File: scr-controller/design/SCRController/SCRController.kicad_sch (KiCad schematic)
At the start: 43 parts, among them J1 VALT, J2 SAL_TRIAC, Q1 2N2907A, Q2 2N2222A, Q3 2N2222A, Q4 2N2907A, U1 TL084, U2 TL084, U3 LM7815_TO220, U4 LM7915_TO220, U5 MOC3011M

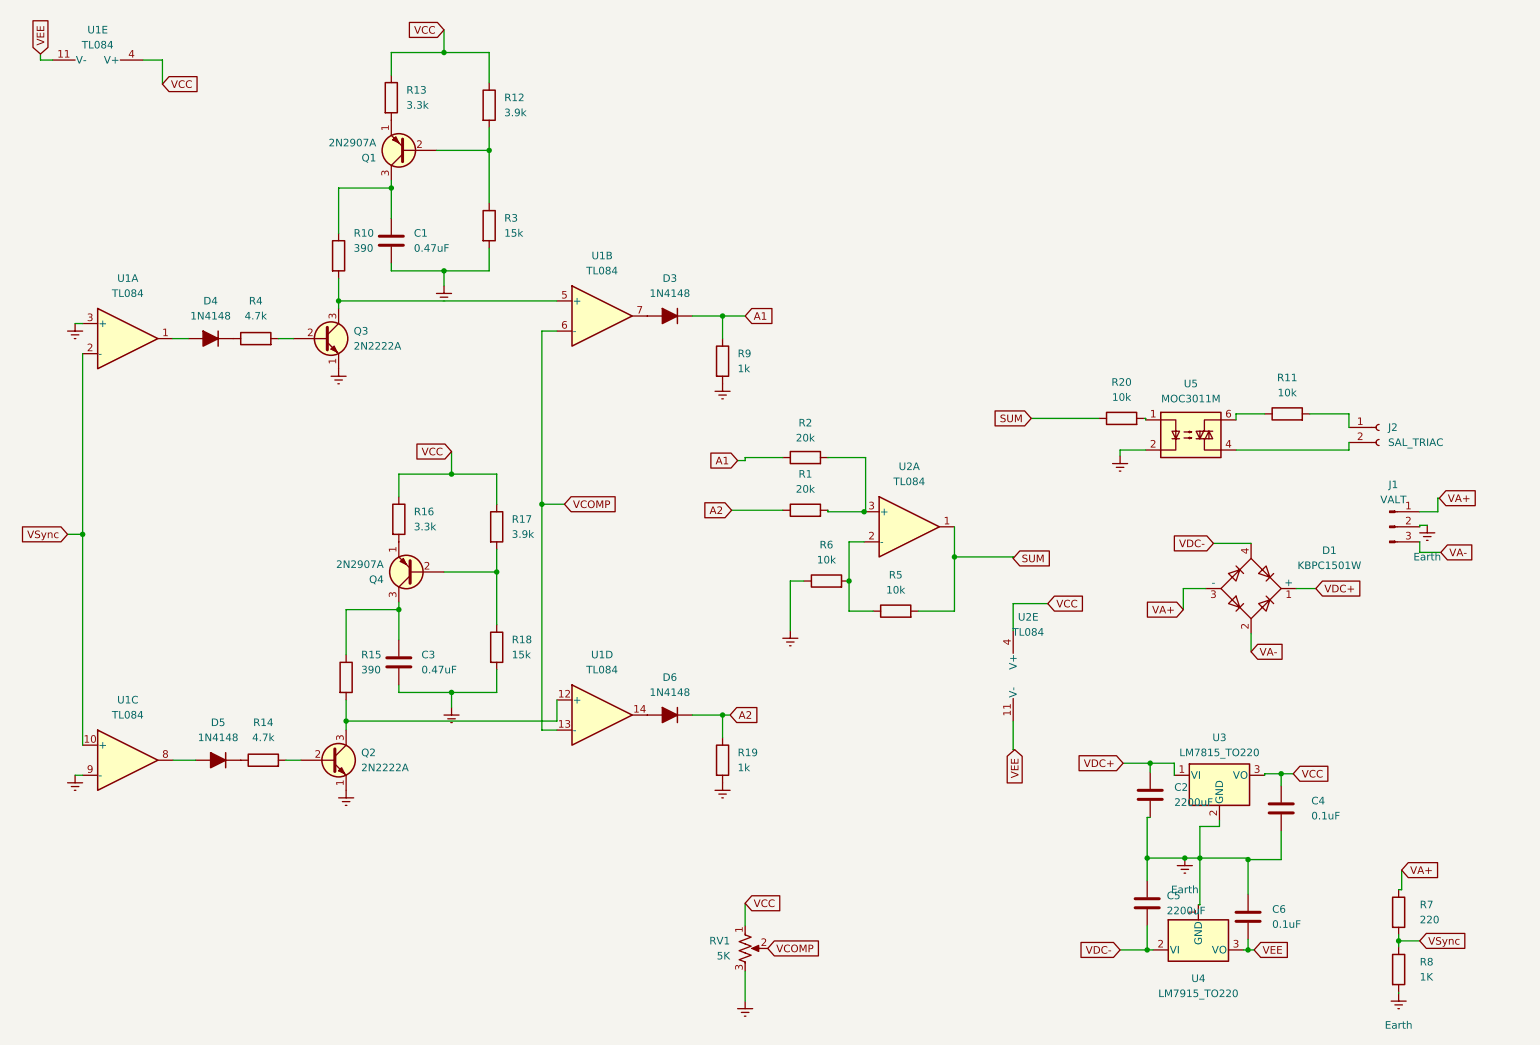
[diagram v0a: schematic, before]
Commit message: feat : Add SCR Controller
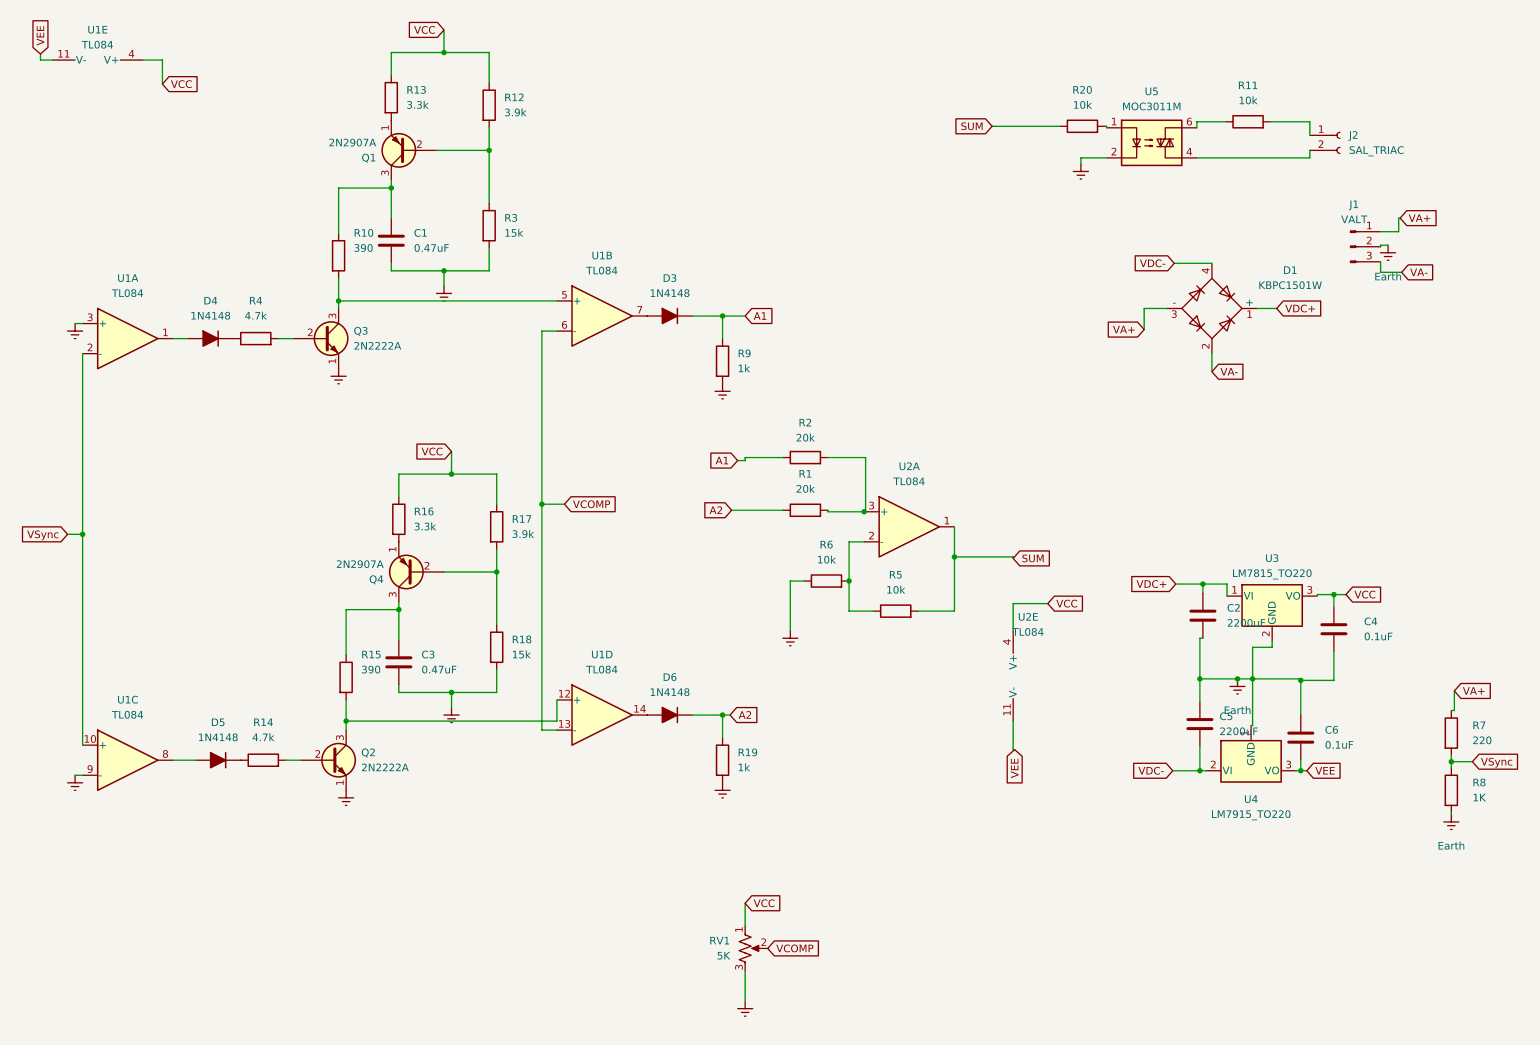
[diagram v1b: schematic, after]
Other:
- moved on the sheet: C2, C4, C5, C6, D1, J1, J2, R11, R20, R7, R8, U3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
